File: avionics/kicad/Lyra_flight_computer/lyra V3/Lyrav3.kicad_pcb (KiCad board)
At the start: 4 copper layers, 25 x 55 mm, 84 parts, among them J2 Screw_Terminal_01x06, J3 Conn_01x02, J4 Conn_01x02, J5 Conn_01x03, J6 Conn_01x06, J7 USB_B_Micro, J8 Conn_01x04, J9 Screw_Terminal_01x06, Q1 AO3401A, Q2 AO3400A, Q3 AO3400A, Q4 AO3400A, Q5 AO3400A, U1 AZ1117-3.3, U2 BMI088, U3 MPL3115A2, U4 ADXL375BCCZ-RL7, U5 LIS3MDL, U6 ADS1015IDGS, U7 W25Q64JVXGIQ, U8 RP2040, X1 S3D12.288000B20F30T

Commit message: real pretrip
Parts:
- removed C28: 100n, Capacitor_SMD:C_0603_1608Metric
- removed R22: 1k, Resistor_SMD:R_0603_1608Metric
- removed U7: W25Q64JVXGIQ, Package_SO:SOIC-8_5.23x5.23mm_P1.27mm
- added C27: 100n, Capacitor_SMD:C_0603_1608Metric, B.Cu at (195.4, 95.6)
- added R14: 1k, Resistor_SMD:R_0603_1608Metric, B.Cu at (201.4, 65.7)
- added U9: W25Q128JVS, Package_SO:SOIC-8_5.23x5.23mm_P1.27mm, B.Cu at (191.5, 99.9)
- moved C4 1.02 mm to (201.5, 69.4), turned to 0 degrees
- moved C3 1.01 mm to (195.5, 69.3), turned to 180 degrees
- moved C10 0.51 mm to (192.5, 68.3)
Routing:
- net /P1 EN : track 31.5 -> 26.7 mm
- net +3V3: track 56.8 -> 60.7 mm, vias 25 -> 23
- net GND: track 84.1 -> 85.8 mm, vias 35 -> 34
- net /QSPI_SS: track 52.2 -> 53.0 mm
- net /LEDRED: track 4.75 -> 5.45 mm
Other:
- board text added: "BOOT"
- board text added: "RST"

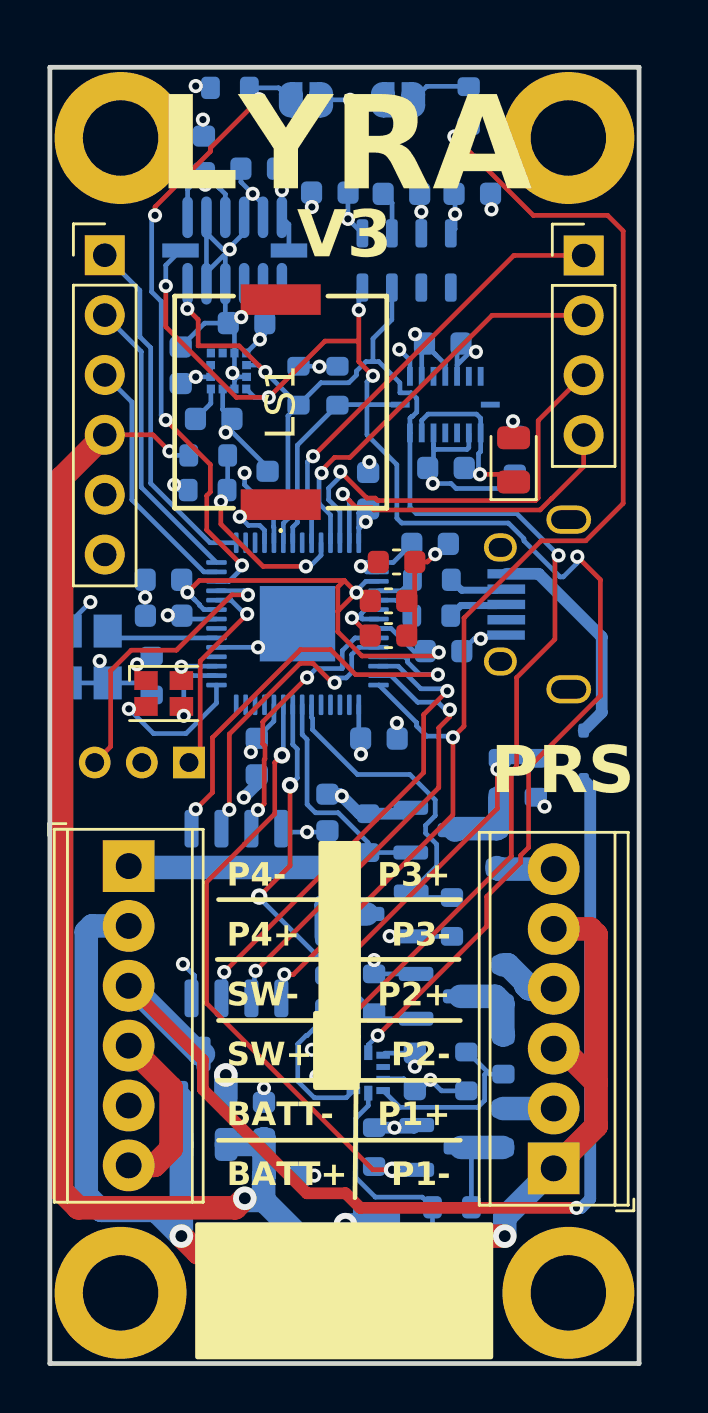
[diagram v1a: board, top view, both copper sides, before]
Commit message: change baro to dps310
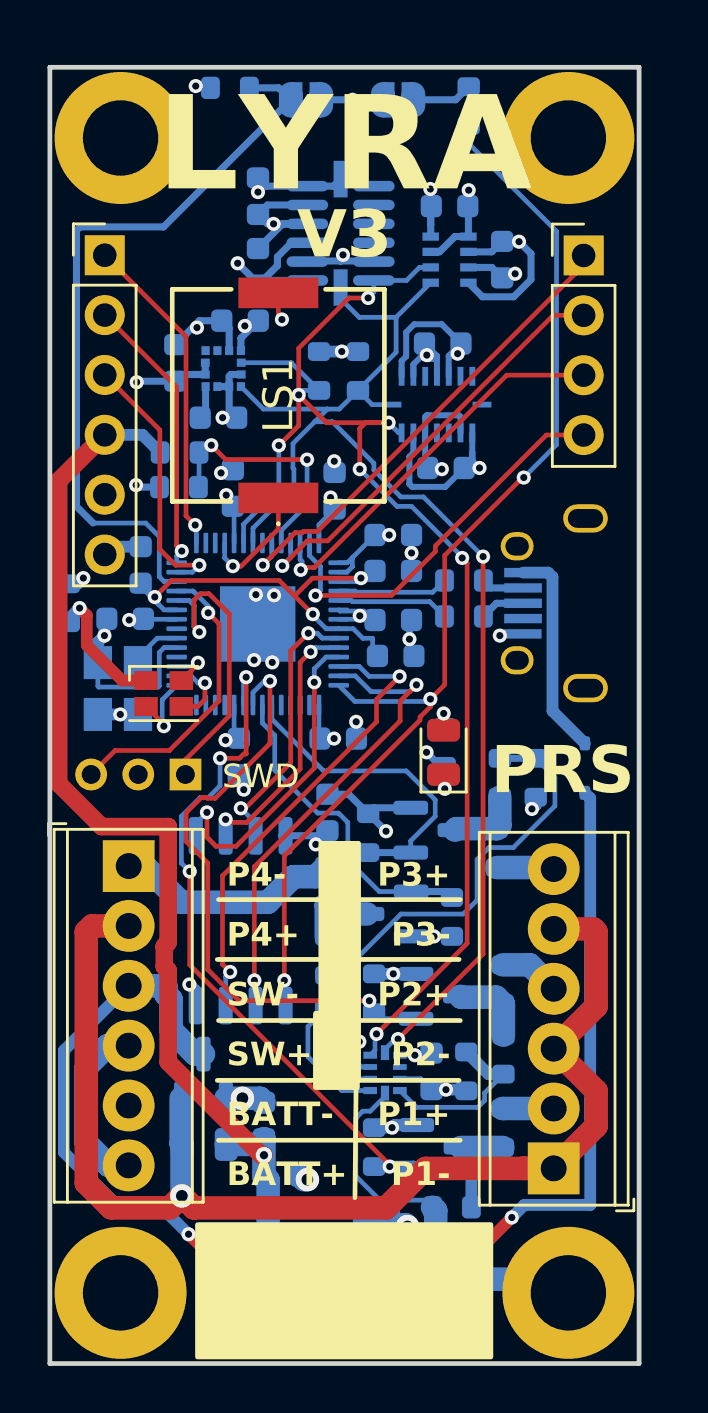
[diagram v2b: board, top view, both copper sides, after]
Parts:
- removed C20, C9: 100n, Capacitor_SMD:C_0603_1608Metric
- removed D3: D, Diode_SMD:D_SOD-323
- removed U3: MPL3115A2, Package_LGA:NXP_LGA-8_3x5mm_P1.25mm_H1.1mm
- added D1: D, Diode_SMD:D_SOD-323, B.Cu at (206.3, 93.8)
- added U7: DPS310XTSA1, easyeda2kicad:LGA-8_DPS310XTSA1, B.Cu at (200.6, 72.2)
- C18, C19: moved to B.Cu
- moved D2 12.8 mm to (200.3, 93.1)
- moved R3 12.8 mm to (200.4, 92.9)
- moved C3 7.85 mm to (202.8, 72.2), turned to 90 degrees
- moved C11 5.30 mm to (192.4, 72.5)
- moved R2 4.67 mm to (184.4, 86.8), turned to 90 degrees
- moved U4 4.55 mm to (195.9, 71.1), turned to 90 degrees
- moved C25 3.59 mm to (198.2, 87.5)
- moved C17 2.04 mm to (198.3, 89.0)
- moved X1 1.85 mm to (186.5, 90.4)
- moved C22 1.73 mm to (195.8, 92.5)
- moved U8 1.69 mm to (192.4, 87.6)
- moved C24 1.64 mm to (186.8, 87.4)
- moved C26 1.47 mm to (191.4, 81.9)
- moved C21 1.42 mm to (195.7, 82.0)
- moved R15 1.39 mm to (201.2, 87.3)
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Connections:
- J7 pad 1: Net-(D3-A) -> VBUS
- U8 pad 6: /P4 EN  -> /P3 EN 
- U8 pad 7: /P3 EN  -> /P4 EN 
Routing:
- net /I2C1 SCL: track 69.8 -> 55.9 mm, vias 6 -> 2
- net Net-(D3-A): track 9.45 -> 0.00 mm
- net +12V: track 46.6 -> 55.9 mm, vias 1 -> 2
- net VBUS: track 0.00 -> 8.96 mm
- net GND: track 85.8 -> 94.3 mm, vias 34 -> 35
- net /P2 EN : track 18.1 -> 25.8 mm
- net +12VA: track 60.9 -> 54.3 mm, vias 2 -> 1
- net +3V3: track 60.7 -> 65.9 mm, vias 23 -> 24
- net /QSPI_SS: track 53.0 -> 47.9 mm
- net /RUN: track 26.8 -> 31.6 mm, vias 4 -> 0
- net /SWCLK: track 8.87 -> 13.0 mm
- net Net-(D4-A): track 1.61 -> 5.65 mm
- net +1V1: track 22.6 -> 18.5 mm
- net /QSPI_SDO: track 17.8 -> 13.8 mm
- net /I2C1 SDA: track 62.1 -> 58.2 mm, vias 4 -> 7
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
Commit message: buasuig
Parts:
- added C9: 1000uf, Capacitor_SMD:CP_Elec_6.3x3.9, F.Cu at (188.3, 89.9)
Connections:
- U7 pad 5: GND -> +3V3
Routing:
- net +1V1: track 18.5 -> 7.80 mm
- added copper zone on F.Cu, net +1V1

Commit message: found new brownout cap
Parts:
- C9: footprint Capacitor_SMD:CP_Elec_6.3x3.9 -> Capacitor_THT:CP_Radial_D8.0mm_P3.80mm
- moved C9 7.43 mm to (195.3, 92.6)
- moved Q1 0.33 mm to (190.1, 107.2)
- moved J5 0.32 mm to (189.2, 94.3)
- moved F1 0.30 mm to (190.1, 110.0)
- moved U9 0.25 mm to (191.7, 100.5)

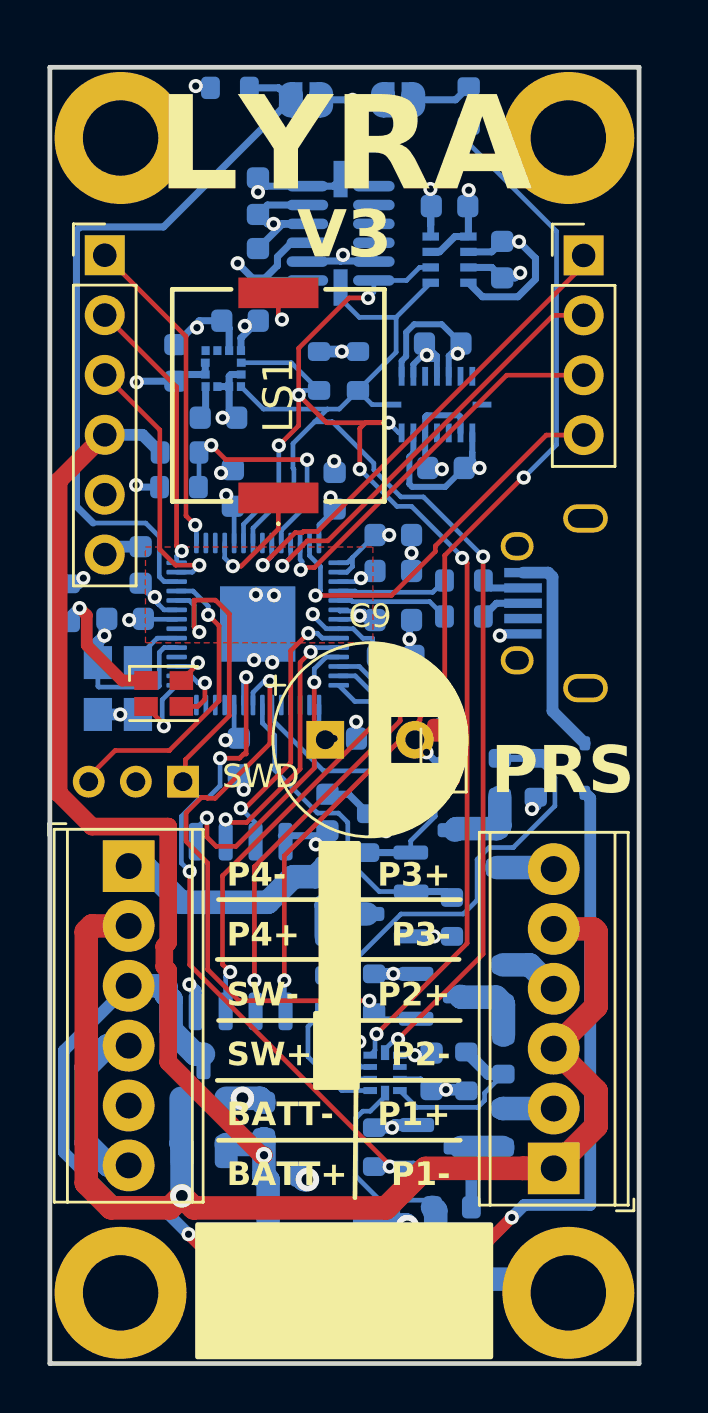
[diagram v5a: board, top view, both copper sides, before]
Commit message: new routing and other stuff
add brownout cap
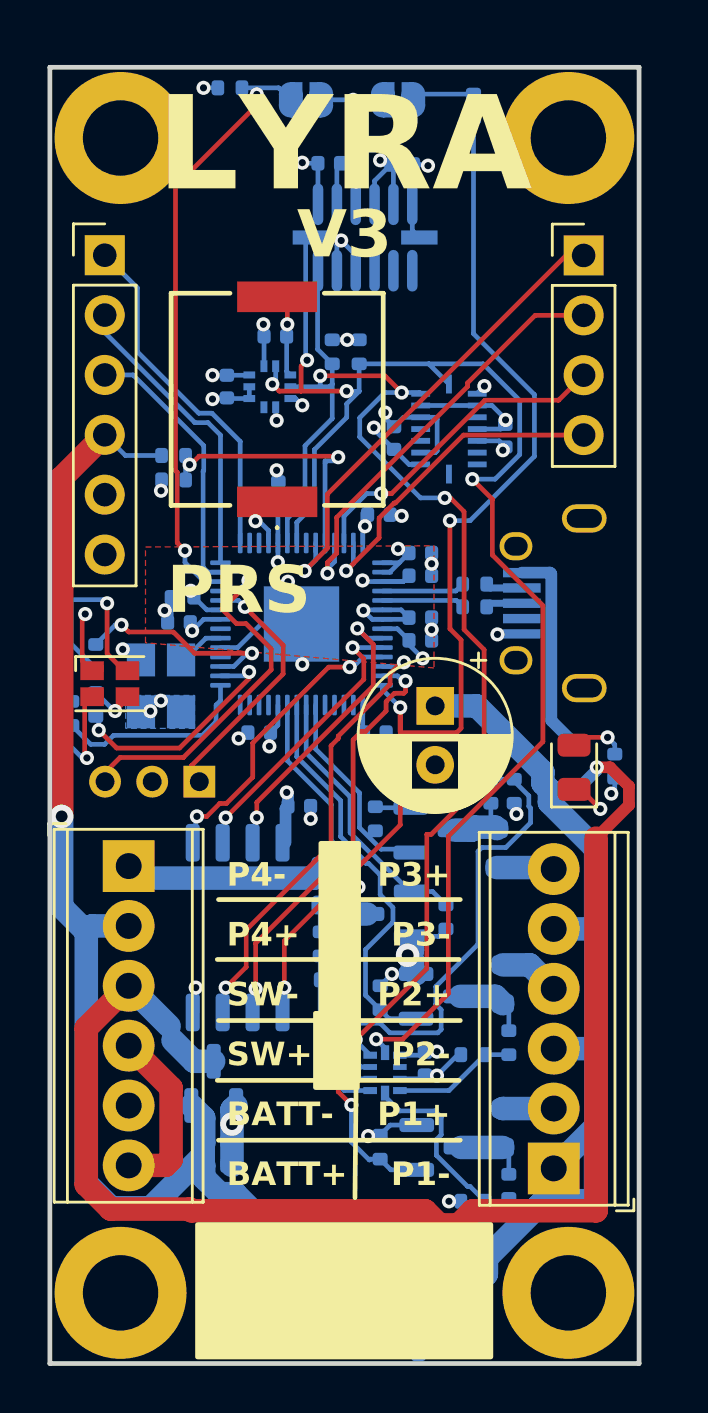
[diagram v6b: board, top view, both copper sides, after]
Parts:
- removed C13, C14, C3: 100n, Capacitor_SMD:C_0603_1608Metric
- removed F1: 200ma, Fuse:Fuse_0805_2012Metric
- removed U5: LIS3MDL, Package_LGA:LGA-12_2x2mm_P0.5mm
- removed U7: DPS310XTSA1, easyeda2kicad:LGA-8_DPS310XTSA1
- added R22: 1k, Resistor_SMD:R_0402_1005Metric, B.Cu at (185.5, 91.1)
- added R28: 1k, Resistor_SMD:R_0402_1005Metric, B.Cu at (185.5, 89.0)
- added U3: BMP388, easyeda2kicad:SENSORM-SMD_BMP388, B.Cu at (192.9, 77.6)
- C1, C10, C11, C15, C16, C17, C18, C19, C2, C21, C22, C23, C24, C25, C26, C27, C5, C6, C7, C8: footprint Capacitor_SMD:C_0603_1608Metric -> Capacitor_SMD:C_0402_1005Metric
- C12: value 1u -> 100n; footprint Capacitor_SMD:C_0603_1608Metric -> Capacitor_SMD:C_0402_1005Metric
- C4: value 10u -> 100n; footprint Capacitor_SMD:C_0603_1608Metric -> Capacitor_SMD:C_0402_1005Metric
- C9: value 1000uf -> 680uf; footprint Capacitor_THT:CP_Radial_D8.0mm_P3.80mm -> Capacitor_THT:CP_Radial_D6.3mm_P2.50mm
- R1, R12, R13, R24, R25, R5: value 6k -> 5.1k; footprint Resistor_SMD:R_0603_1608Metric -> Resistor_SMD:R_0402_1005Metric
- R10, R11, R21, R23, R4: value 20k -> 15k; footprint Resistor_SMD:R_0603_1608Metric -> Resistor_SMD:R_0402_1005Metric
- R14, R16, R17, R2, R26, R27, R3, R6, R7: footprint Resistor_SMD:R_0603_1608Metric -> Resistor_SMD:R_0402_1005Metric
- R15, R18: value 27R -> 22R; footprint Resistor_SMD:R_0603_1608Metric -> Resistor_SMD:R_0402_1005Metric
- R19, R20, R8, R9: value 10R -> 1R
- moved C4 12.2 mm to (191.1, 77.6), turned to -90 degrees
- moved R3 7.26 mm to (207.6, 93.7)
- moved C10 6.27 mm to (198.6, 68.1), turned to 180 degrees
- moved D2 5.57 mm to (205.8, 93.7)
- moved C11 5.33 mm to (195.5, 68.1), turned to 0 degrees
- moved C9 4.88 mm to (199.9, 91.1), turned to -90 degrees
- moved C2 4.73 mm to (202.9, 79.7), turned to 90 degrees
- moved R2 4.68 mm to (184.5, 91.4)
- moved C12 4.39 mm to (193.2, 75.4), turned to 0 degrees
- moved C7 2.85 mm to (190.6, 110.6)
- moved R10 2.57 mm to (203.1, 111.5), turned to -90 degrees
- moved C1 2.54 mm to (198.2, 79.8), turned to -90 degrees
- moved D4 2.32 mm to (186.1, 90.2)
- moved C24 2.29 mm to (189.1, 87.6)
- moved C16 2.25 mm to (189.2, 86.5), turned to 180 degrees
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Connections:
- C5 pad 1: +12VA -> +12P
- C7 pad 1: +12VA -> +12P
- C8 pad 1: +12VA -> +12P
- C9 pad 1: +12VA -> +12P
- D4 pad 1: Net-(D4-A) -> +3V3
- D4 pad 2: /LEDRED -> Net-(D4-RK)
- D4 pad 3: /LEDGREEN -> Net-(D4-GK)
- D4 pad 4: /LEDBLUE -> Net-(D4-BK)
- J6 pad 4: +12VA -> +12P
- R2 pad 1: Net-(D4-A) -> /LEDRED
- R2 pad 2: +3V3 -> Net-(D4-RK)
- R4 pad 1: +12VA -> +12P
- U1 pad 3: +12VA -> +12P
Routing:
- net +12VA: track 54.5 -> 0.00 mm, vias 1 -> 0
- net +12P: track 53.6 -> 103.3 mm
- net GND: track 94.6 -> 65.5 mm
- net +3V3: track 66.1 -> 45.8 mm, vias 24 -> 26
- net /P2 EN : track 25.8 -> 17.1 mm, vias 2 -> 0
- net Net-(D4-BK): track 0.00 -> 8.25 mm, vias 0 -> 1
- net /LEDBLUE: track 2.01 -> 9.04 mm, vias 1 -> 2
- net /LEDGREEN: track 3.14 -> 10.1 mm, vias 1 -> 2
- net /I2C1 SCL: track 55.9 -> 62.8 mm, vias 2 -> 5
- net /RUN: track 31.6 -> 25.0 mm, vias 0 -> 2
- net Net-(D4-RK): track 0.00 -> 6.07 mm, vias 0 -> 1
- net /P1 EN : track 29.4 -> 23.7 mm, vias 4 -> 2
- net Net-(D4-A): track 5.65 -> 0.00 mm, vias 1 -> 0
- net /LEDRED: track 3.17 -> 8.47 mm, vias 1 -> 0
- net /P3 EN : track 13.4 -> 8.58 mm
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- added copper zone on B.Cu, net +3V3
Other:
- board text removed: "SWD"
